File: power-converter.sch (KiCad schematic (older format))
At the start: 11 parts

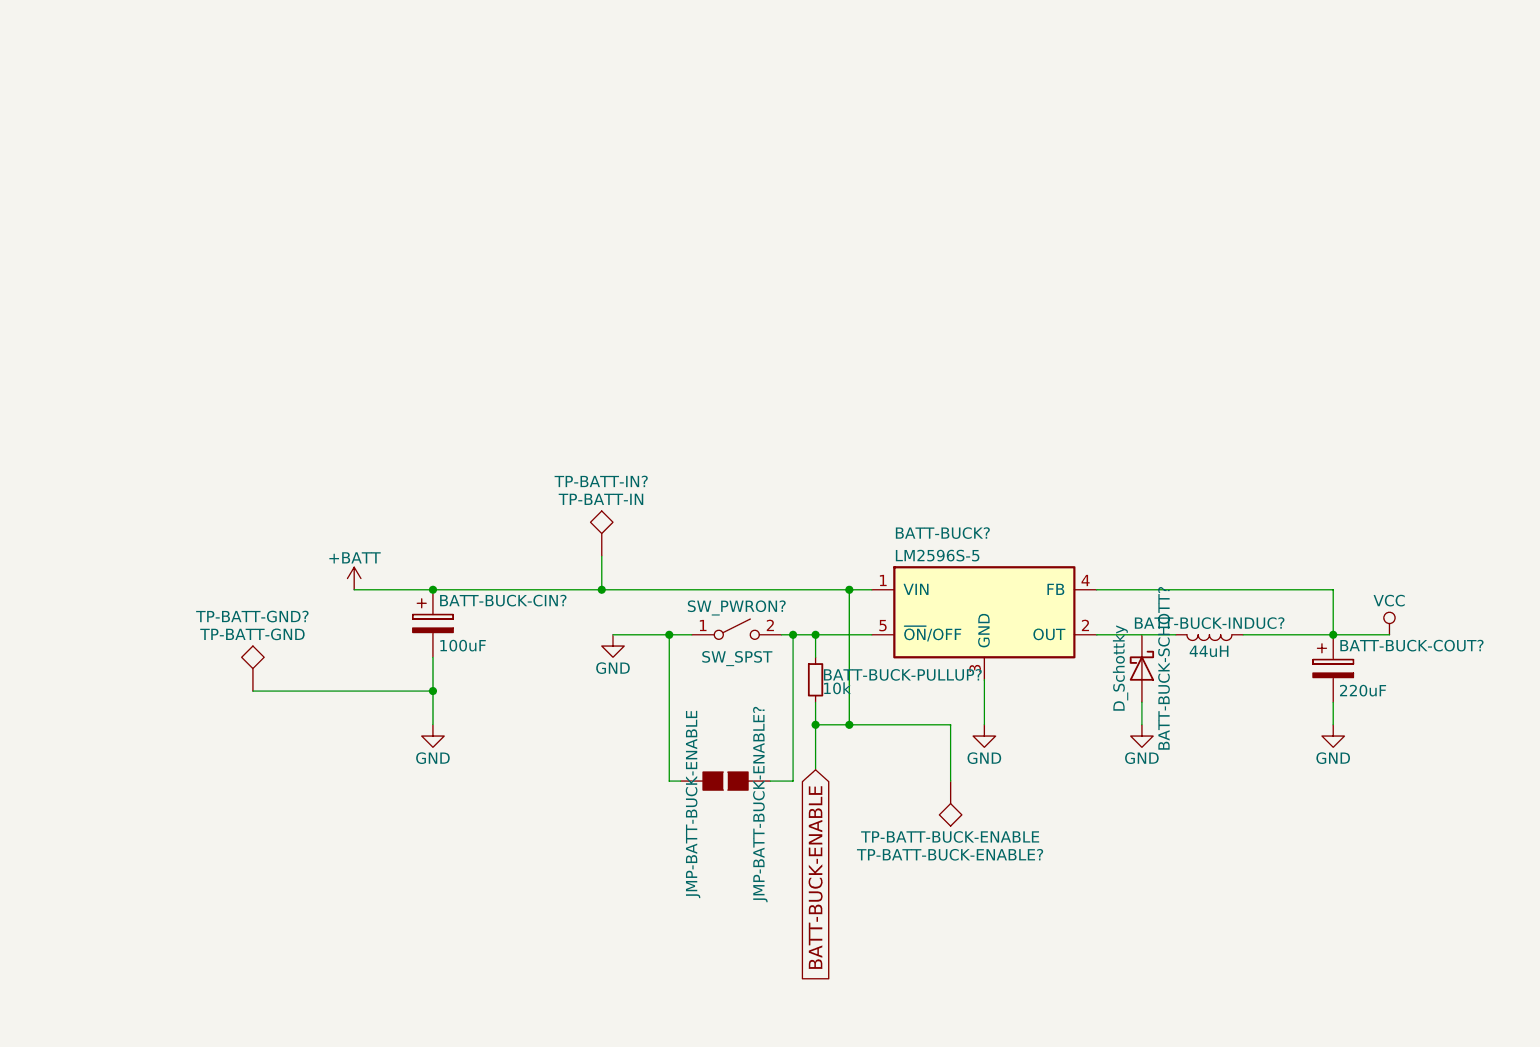
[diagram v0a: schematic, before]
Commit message: mpu6000 circuit complete + power circuit extracted + other changes
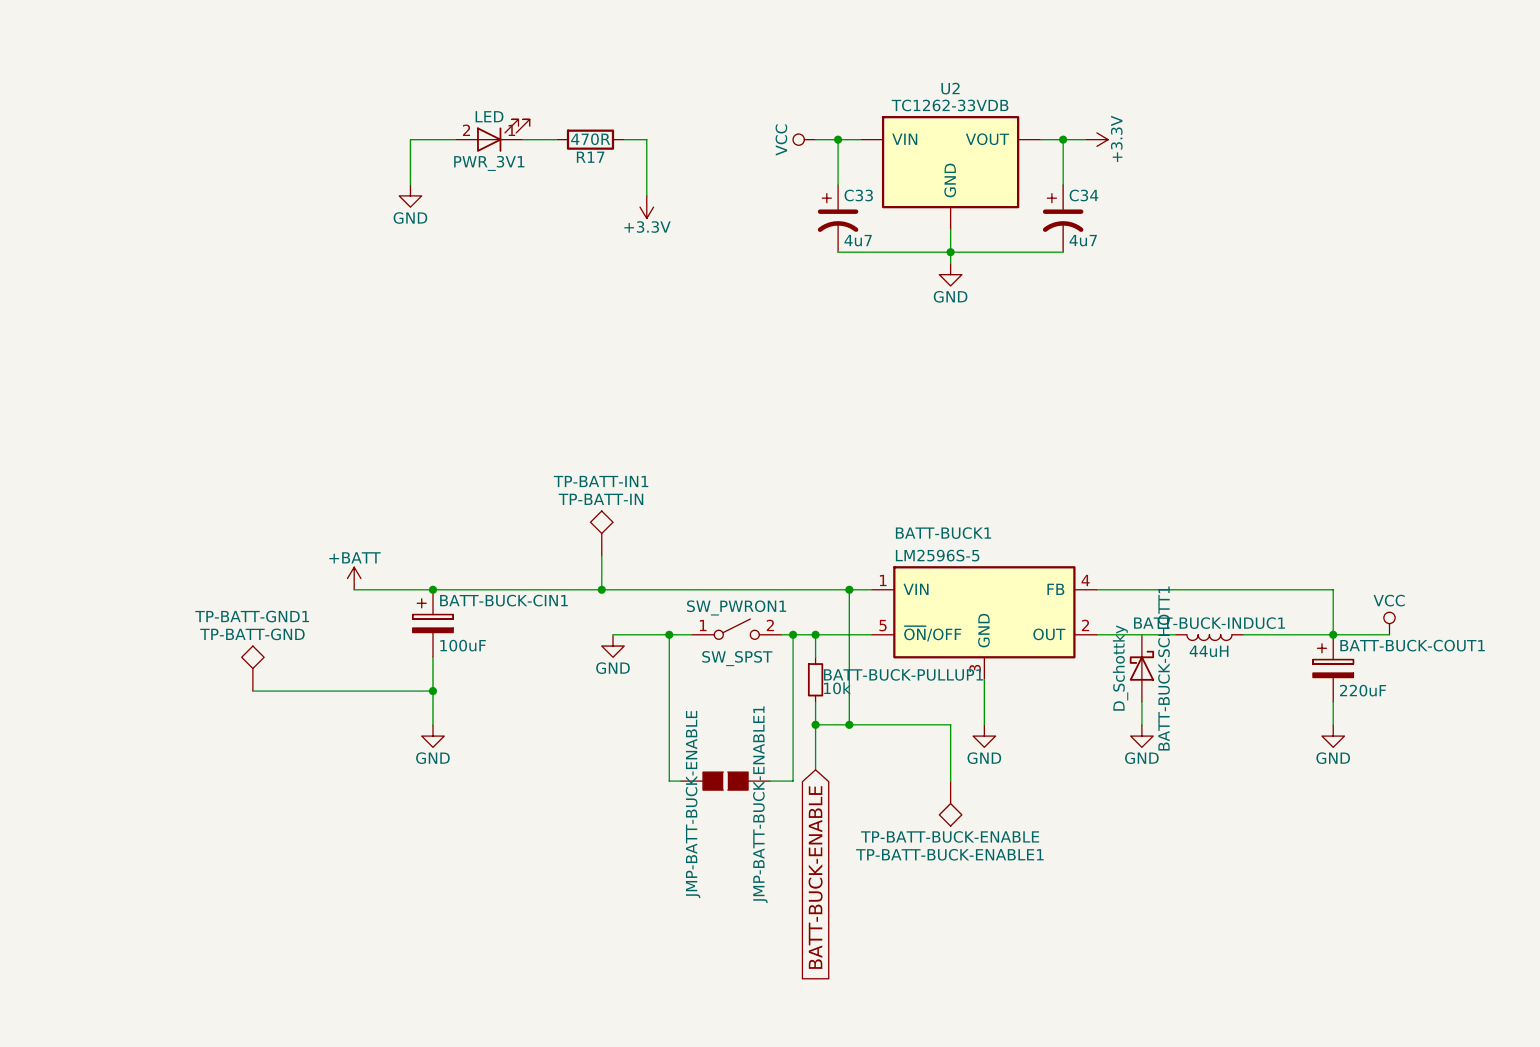
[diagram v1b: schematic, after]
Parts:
- added C33, C34: 4u7, symbol CP1
- added PWR_3V1: LED, LEDs:LED_0603, symbol LED
- added R17: 470R, Resistors_SMD:R_0603, symbol R
- added U2: TC1262-33VDB, TO_SOT_Packages_SMD:SOT-223, symbol TC1262-33VDB
- gave numbers to parts that had none: 11
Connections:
- net GND: now also C33.2, C34.2, PWR_3V1.2 (A), U2.2 (GND), U2.4 (GND)
- net VCC: now also C33.1, U2.1 (VIN)
- new net: PWR_3V1.1 (K), R17.2
- new net +3V3: C34.1, R17.1, U2.3 (VOUT)
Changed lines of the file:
@@
 $Descr A4 11693 8268
 encoding utf-8
-Sheet 3 3
+Sheet 3 5
 Title "Power Converter"
 Date ""
@@
 $EndDescr
 $Comp
-L LM2596S-5 BATT-BUCK?
+L LM2596S-5 BATT-BUCK1
 U 1 1 5B2D2C26
 P 6650 3800
-F 0 "BATT-BUCK?" H 6250 4150 50  0000 L CNN
+F 0 "BATT-BUCK1" H 6250 4150 50  0000 L CNN
 F 1 "LM2596S-5" H 6250 4050 50  0000 L CNN
 F 2 "TO_SOT_Packages_SMD:TO-263-5Lead" H 6950 3550 50  0001 C CIN
@@
 $EndComp
 $Comp
-L SW_SPST SW_PWRON?
+L SW_SPST SW_PWRON1
 U 1 1 5B2D2C2D
 P 5550 3900
-F 0 "SW_PWRON?" H 5550 4025 50  0000 C CNN
+F 0 "SW_PWRON1" H 5550 4025 50  0000 C CNN
 F 1 "SW_SPST" H 5550 3800 50  0000 C CNN
 F 2 "Buttons_Switches_SMD:SW_SPST_EVQQ2" H 5550 3900 50  0001 C CNN
@@
 	5750 3900 6150 3900
 $Comp
-L GND #PWR?
+L GND #PWR1232
 U 1 1 5B2D2C35
 P 5000 3900
-F 0 "#PWR?" H 5000 3650 50  0001 C CNN
+F 0 "#PWR1232" H 5000 3650 50  0001 C CNN
 F 1 "GND" H 5000 3750 50  0000 C CNN
 F 2 "" H 5000 3900 50  0001 C CNN
@@
 	5000 3900 5350 3900
 $Comp
-L L BATT-BUCK-INDUC?
+L L BATT-BUCK-INDUC1
 U 1 1 5B2D2C3C
 P 7650 3900
-F 0 "BATT-BUCK-INDUC?" V 7600 3900 50  0000 C CNN
+F 0 "BATT-BUCK-INDUC1" V 7600 3900 50  0000 C CNN
 F 1 "44uH" V 7725 3900 50  0000 C CNN
 F 2 "" H 7650 3900 50  0001 C CNN
@@
 	7150 3900 7500 3900
 $Comp
-L VCC #PWR?
+L VCC #PWR1240
 U 1 1 5B2D2C44
 P 8450 3900
-F 0 "#PWR?" H 8450 3750 50  0001 C CNN
+F 0 "#PWR1240" H 8450 3750 50  0001 C CNN
 F 1 "VCC" H 8450 4050 50  0000 C CNN
 F 2 "" H 8450 3900 50  0001 C CNN
@@
 Connection ~ 8200 3900
 $Comp
-L D_Schottky BATT-BUCK-SCHOTT?
+L D_Schottky BATT-BUCK-SCHOTT1
 U 1 1 5B2D2C4E
 P 7350 4050
-F 0 "BATT-BUCK-SCHOTT?" H 7350 4150 50  0000 C CNN
+F 0 "BATT-BUCK-SCHOTT1" H 7350 4150 50  0000 C CNN
 F 1 "D_Schottky" H 7350 3950 50  0000 C CNN
 F 2 "" H 7350 4050 50  0001 C CNN
@@
 $EndComp
 $Comp
-L GND #PWR?
+L GND #PWR1238
 U 1 1 5B2D2C55
 P 7350 4300
-F 0 "#PWR?" H 7350 4050 50  0001 C CNN
+F 0 "#PWR1238" H 7350 4050 50  0001 C CNN
 F 1 "GND" H 7350 4150 50  0000 C CNN
 F 2 "" H 7350 4300 50  0001 C CNN
@@
 	7350 4200 7350 4300
 $Comp
-L CP BATT-BUCK-COUT?
+L CP BATT-BUCK-COUT1
 U 1 1 5B2D2C5C
 P 8200 4050
-F 0 "BATT-BUCK-COUT?" H 8225 4150 50  0000 L CNN
+F 0 "BATT-BUCK-COUT1" H 8225 4150 50  0000 L CNN
 F 1 "220uF" H 8225 3950 50  0000 L CNN
 F 2 "" H 8238 3900 50  0001 C CNN
@@
 $EndComp
 $Comp
-L GND #PWR?
+L GND #PWR1239
 U 1 1 5B2D2C63
 P 8200 4300
-F 0 "#PWR?" H 8200 4050 50  0001 C CNN
+F 0 "#PWR1239" H 8200 4050 50  0001 C CNN
 F 1 "GND" H 8200 4150 50  0000 C CNN
 F 2 "" H 8200 4300 50  0001 C CNN
@@
 	8200 4200 8200 4300
 $Comp
-L GND #PWR?
+L GND #PWR1236
 U 1 1 5B2D2C6A
 P 6650 4300
-F 0 "#PWR?" H 6650 4050 50  0001 C CNN
+F 0 "#PWR1236" H 6650 4050 50  0001 C CNN
 F 1 "GND" H 6650 4150 50  0000 C CNN
 F 2 "" H 6650 4300 50  0001 C CNN
@@
 	6650 4100 6650 4300
 $Comp
-L CP BATT-BUCK-CIN?
+L CP BATT-BUCK-CIN1
 U 1 1 5B2D2C71
 P 4200 3850
-F 0 "BATT-BUCK-CIN?" H 4225 3950 50  0000 L CNN
+F 0 "BATT-BUCK-CIN1" H 4225 3950 50  0000 L CNN
 F 1 "100uF" H 4225 3750 50  0000 L CNN
 F 2 "" H 4238 3700 50  0001 C CNN
@@
 	3850 3700 6150 3700
 $Comp
-L GND #PWR?
+L GND #PWR1231
 U 1 1 5B2D2C79
 P 4200 4300
-F 0 "#PWR?" H 4200 4050 50  0001 C CNN
+F 0 "#PWR1231" H 4200 4050 50  0001 C CNN
 F 1 "GND" H 4200 4150 50  0000 C CNN
 F 2 "" H 4200 4300 50  0001 C CNN
@@
 	4200 4000 4200 4300
 $Comp
-L R_Small BATT-BUCK-PULLUP?
+L R_Small BATT-BUCK-PULLUP1
 U 1 1 5B2D2C80
 P 5900 4100
-F 0 "BATT-BUCK-PULLUP?" H 5930 4120 50  0000 L CNN
+F 0 "BATT-BUCK-PULLUP1" H 5930 4120 50  0000 L CNN
 F 1 "10k" H 5930 4060 50  0000 L CNN
 F 2 "" H 5900 4100 50  0001 C CNN
@@
 Connection ~ 5900 4300
 $Comp
-L GS2 JMP-BATT-BUCK-ENABLE?
+L GS2 JMP-BATT-BUCK-ENABLE1
 U 1 1 5B2D2C8C
 P 5500 4550
-F 0 "JMP-BATT-BUCK-ENABLE?" H 5600 4700 50  0000 C CNN
+F 0 "JMP-BATT-BUCK-ENABLE1" H 5600 4700 50  0000 C CNN
 F 1 "JMP-BATT-BUCK-ENABLE" H 5600 4401 50  0000 C CNN
 F 2 "Connectors:GS2" V 5574 4550 50  0001 C CNN
@@
 Connection ~ 5800 3900
 $Comp
-L TEST TP-BATT-BUCK-ENABLE?
+L TEST TP-BATT-BUCK-ENABLE1
 U 1 1 5B2D2C9C
 P 6500 4550
-F 0 "TP-BATT-BUCK-ENABLE?" H 6500 4850 50  0000 C BNN
+F 0 "TP-BATT-BUCK-ENABLE1" H 6500 4850 50  0000 C BNN
 F 1 "TP-BATT-BUCK-ENABLE" H 6500 4800 50  0000 C CNN
 F 2 "" H 6500 4550 50  0001 C CNN
@@
 Connection ~ 6050 4300
 $Comp
-L +BATT #PWR?
+L +BATT #PWR1229
 U 1 1 5B2D2CA5
 P 3850 3700
-F 0 "#PWR?" H 3850 3550 50  0001 C CNN
+F 0 "#PWR1229" H 3850 3550 50  0001 C CNN
 F 1 "+BATT" H 3850 3840 50  0000 C CNN
 F 2 "" H 3850 3700 50  0001 C CNN
@@
 Connection ~ 4200 3700
 $Comp
-L TEST TP-BATT-IN?
+L TEST TP-BATT-IN1
 U 1 1 5B2D2CAC
 P 4950 3550
-F 0 "TP-BATT-IN?" H 4950 3850 50  0000 C BNN
+F 0 "TP-BATT-IN1" H 4950 3850 50  0000 C BNN
 F 1 "TP-BATT-IN" H 4950 3800 50  0000 C CNN
 F 2 "" H 4950 3550 50  0001 C CNN
@@
 Connection ~ 4950 3700
 $Comp
-L TEST TP-BATT-GND?
+L TEST TP-BATT-GND1
 U 1 1 5B2D2CB5
 P 3400 4150
-F 0 "TP-BATT-GND?" H 3400 4450 50  0000 C BNN
+F 0 "TP-BATT-GND1" H 3400 4450 50  0000 C BNN
 F 1 "TP-BATT-GND" H 3400 4400 50  0000 C CNN
 F 2 "" H 3400 4150 50  0001 C CNN
@@
 	3400 4150 4200 4150
 Connection ~ 4200 4150
+$Comp
+L +3.3V #PWR1233
+U 1 1 5B2DAE29
+P 5150 1950
+F 0 "#PWR1233" H 5150 1800 50  0001 C CNN
+F 1 "+3.3V" H 5150 2090 50  0000 C CNN
+F 2 "" H 5150 1950 50  0001 C CNN
+F 3 "" H 5150 1950 50  0001 C CNN
+	1    5150 1950
+	-1   0    0    1
+$EndComp
+$Comp
+L TC1262-33VDB U2
+U 1 1 5B2DAE2F
+P 6500 1800
+F 0 "U2" H 6500 2125 50  0000 C CNN
+F 1 "TC1262-33VDB" H 6500 2050 50  0000 C CNN
+F 2 "TO_SOT_Packages_SMD:SOT-223" H 6550 1550 50  0001 L CIN
+F 3 "" H 6500 1600 50  0001 C CNN
+	1    6500 1800
+	1    0    0    -1
+$EndComp
+$Comp
+L +3.3V #PWR1237
+U 1 1 5B2DAE36
+P 7100 1700
+F 0 "#PWR1237" H 7100 1550 50  0001 C CNN
+F 1 "+3.3V" H 7100 1840 50  0000 C CNN
+F 2 "" H 7100 1700 50  0001 C CNN
+F 3 "" H 7100 1700 50  0001 C CNN
+	1    7100 1700
+	0    1    1    0
+$EndComp
+$Comp
+L VCC #PWR1234
+U 1 1 5B2DAE3C
+P 5900 1700
+F 0 "#PWR1234" H 5900 1550 50  0001 C CNN
+F 1 "VCC" H 5900 1850 50  0000 C CNN
+F 2 "" H 5900 1700 50  0001 C CNN
+F 3 "" H 5900 1700 50  0001 C CNN
+	1    5900 1700
+	0    -1   -1   0
+$EndComp
+$Comp
+L GND #PWR1235
+U 1 1 5B2DAE42
+P 6500 2250
+F 0 "#PWR1235" H 6500 2000 50  0001 C CNN
+F 1 "GND" H 6500 2100 50  0000 C CNN
+F 2 "" H 6500 2250 50  0001 C CNN
+F 3 "" H 6500 2250 50  0001 C CNN
+	1    6500 2250
+	1    0    0    -1
+$EndComp
+$Comp
+L R R17
+U 1 1 5B2DAE48
+P 4900 1700
+F 0 "R17" V 4980 1700 50  0000 C CNN
+F 1 "470R" V 4900 1700 50  0000 C CNN
+F 2 "Resistors_SMD:R_0603" V 4830 1700 50  0001 C CNN
+F 3 "" H 4900 1700 50  0001 C CNN
+	1    4900 1700
+	0    1    1    0
+$EndComp
+$Comp
+L GND #PWR1230
+U 1 1 5B2DAE4F
+P 4100 1900
+F 0 "#PWR1230" H 4100 1650 50  0001 C CNN
+F 1 "GND" H 4100 1750 50  0000 C CNN
+F 2 "" H 4100 1900 50  0001 C CNN
+F 3 "" H 4100 1900 50  0001 C CNN
+	1    4100 1900
+	1    0    0    -1
+$EndComp
+$Comp
+L LED PWR_3V1
+U 1 1 5B2DAE55
+P 4450 1700
+F 0 "PWR_3V1" H 4450 1800 50  0000 C CNN
+F 1 "LED" H 4450 1600 50  0000 C CNN
+F 2 "LEDs:LED_0603" H 4450 1700 50  0001 C CNN
+F 3 "" H 4450 1700 50  0001 C CNN
+	1    4450 1700
+	-1   0    0    1
+$EndComp
+$Comp
+L CP1 C33
+U 1 1 5B2DAE5C
+P 6000 2050
+F 0 "C33" H 6025 2150 50  0000 L CNN
+F 1 "4u7" H 6025 1950 50  0000 L CNN
+F 2 "" H 6000 2050 50  0001 C CNN
+F 3 "" H 6000 2050 50  0001 C CNN
+	1    6000 2050
+	1    0    0    -1
+$EndComp
+$Comp
+L CP1 C34
+U 1 1 5B2DAE63
+P 7000 2050
+F 0 "C34" H 7025 2150 50  0000 L CNN
+F 1 "4u7" H 7025 1950 50  0000 L CNN
+F 2 "" H 7000 2050 50  0001 C CNN
+F 3 "" H 7000 2050 50  0001 C CNN
+	1    7000 2050
+	1    0    0    -1
+$EndComp
+Wire Wire Line
+	6500 2100 6500 2250
+Wire Wire Line
+	5900 1700 6100 1700
+Wire Wire Line
+	6900 1700 7100 1700
+Wire Wire Line
+	4600 1700 4750 1700
+Wire Wire Line
+	5150 1700 5150 1950
+Wire Wire Line
+	5050 1700 5150 1700
+Wire Wire Line
+	4100 1700 4100 1900
+Wire Wire Line
+	4300 1700 4100 1700
+Wire Wire Line
+	7000 1900 7000 1700
+Connection ~ 7000 1700
+Wire Wire Line
+	6000 2200 7000 2200
+Connection ~ 6500 2200
+Wire Wire Line
+	6000 1900 6000 1700
+Connection ~ 6000 1700
 $EndSCHEMATC
